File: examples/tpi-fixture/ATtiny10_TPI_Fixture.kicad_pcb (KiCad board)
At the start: 2 copper layers, 76.2 x 63.5 mm, 25 parts, among them J1 USBasp ISP (2x5 box header), J2 CNV-SOT23-6L-DIP carrier, SW1A 4PDT on-on (pole A), SW1B 4PDT on-on (pole B), SW1C 4PDT on-on (pole C), SW1D 4PDT on-on (pole D), SW2 MODE NORMAL/HV, SW3 HV POWER, SW4 HV ENABLE (guarded)

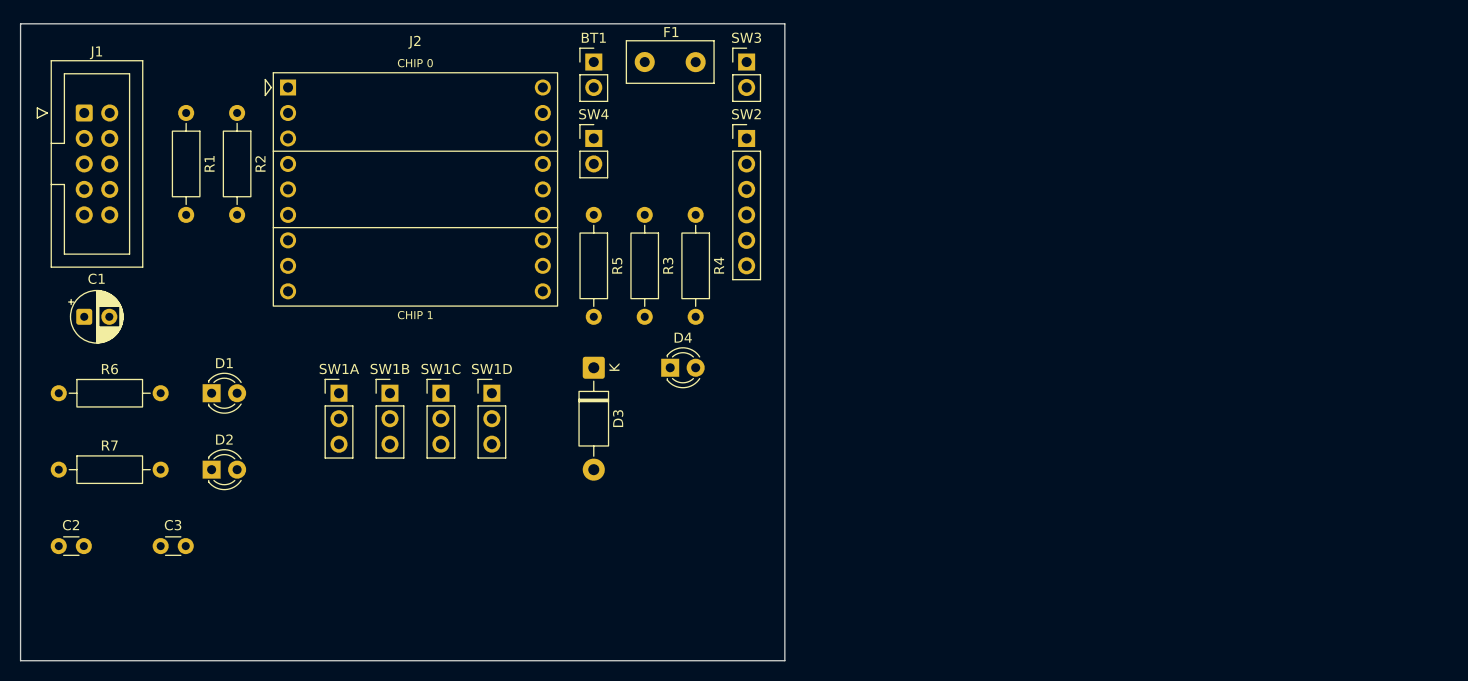
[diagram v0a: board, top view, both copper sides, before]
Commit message: Make examples/tpi-fixture the real-parts board (fixture by Mildrew) and test it
The board and netlist are Mildrew's real-parts version (22 footprints, 86 pads, 41 nets), copied
byte-exactly. New tests: all 22 parts snap with examples/x56.toml, BT1 passes as slotted (and is
rejected without it), 0 conflicts, the netlist matches, and the X56 grid-width warning is present
(the outline is still 30 holes wide).
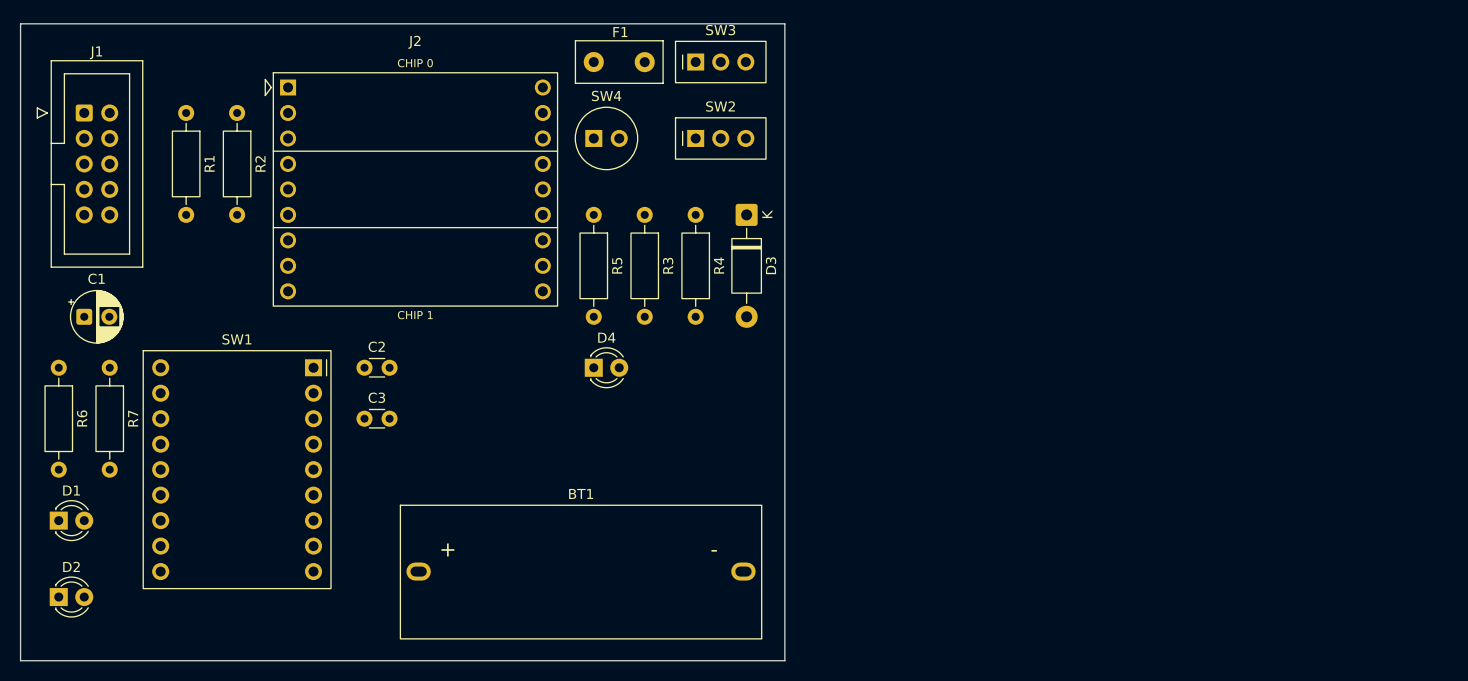
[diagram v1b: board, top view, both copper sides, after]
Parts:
- removed SW1A: 4PDT on-on (pole A), Connector_PinHeader_2.54mm:PinHeader_1x03_P2.54mm_Vertical
- removed SW1B: 4PDT on-on (pole B), Connector_PinHeader_2.54mm:PinHeader_1x03_P2.54mm_Vertical
- removed SW1C: 4PDT on-on (pole C), Connector_PinHeader_2.54mm:PinHeader_1x03_P2.54mm_Vertical
- removed SW1D: 4PDT on-on (pole D), Connector_PinHeader_2.54mm:PinHeader_1x03_P2.54mm_Vertical
- added SW1: CHIP SEL 6PDT (MSS6200 on adapter), ATtiny10_TPI_Fixture:MSS6200_Adapter_2x09_P2.54mm, F.Cu at (79.2, 84.3)
- BT1: value 12V (23A or 8xAA pack) -> 12V 23A cell (MPD BH23APC); footprint Connector_PinHeader_2.54mm:PinHeader_1x02_P2.54mm_Vertical -> ATtiny10_TPI_Fixture:BatteryHolder_MPD_BH23APC_1x23A_Stripboard_H0-H13
- SW2: footprint Connector_PinHeader_2.54mm:PinHeader_1x06_P2.54mm_Vertical -> ATtiny10_TPI_Fixture:SW_Slide_SPDT_SS12D00G_P2.50mm_Vertical
- SW3: footprint Connector_PinHeader_2.54mm:PinHeader_1x02_P2.54mm_Vertical -> ATtiny10_TPI_Fixture:SW_Slide_SPDT_SS12D00G_P2.50mm_Vertical
- SW4: footprint Connector_PinHeader_2.54mm:PinHeader_1x02_P2.54mm_Vertical -> ATtiny10_TPI_Fixture:SW_Push_Round_D6mm_1x02_P2.54mm_PROVISIONAL
- moved BT1 53.8 mm to (89.4, 104.6)
- moved C2 35.3 mm to (84.3, 84.3)
- moved C3 24.0 mm to (84.3, 89.4)
- moved D3 21.6 mm to (122.4, 69.0)
- moved D1 19.8 mm to (53.8, 99.5)
- moved D2 19.8 mm to (53.8, 107.2)
- moved R7 11.4 mm to (58.9, 84.3), turned to -90 degrees
- moved D4 7.62 mm to (107.2, 84.3)
- moved F1 5.08 mm to (107.2, 53.8)
- moved SW2 5.08 mm to (117.3, 61.4)
- moved SW3 5.08 mm to (117.3, 53.8)
- moved R6 2.54 mm to (53.8, 84.3), turned to -90 degrees
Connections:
- F1 pad 2: Net-(SW3-A) -> Net-(SW3-B)
- R3 pad 1: /SCHEMATIC DIAGRAM/HV_ARMED -> /SCHEMATIC DIAGRAM/HV_SW
- SW4 pad 1: Net-(SW3-B) -> Net-(SW3-A)

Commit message: Update the real-parts fixture: X56 outline, BT1 up one strip (fixture by Mildrew)
Mildrew widened the Edge.Cuts outline to Kevin's X56 board (56 x 24 holes, A1-X56) and moved BT1
up one strip (slot jobs now on strip U). The X56 grid-width warning is gone; build writes the
full 56-hole strips (1226 tracks). Tests and the fixture README updated.
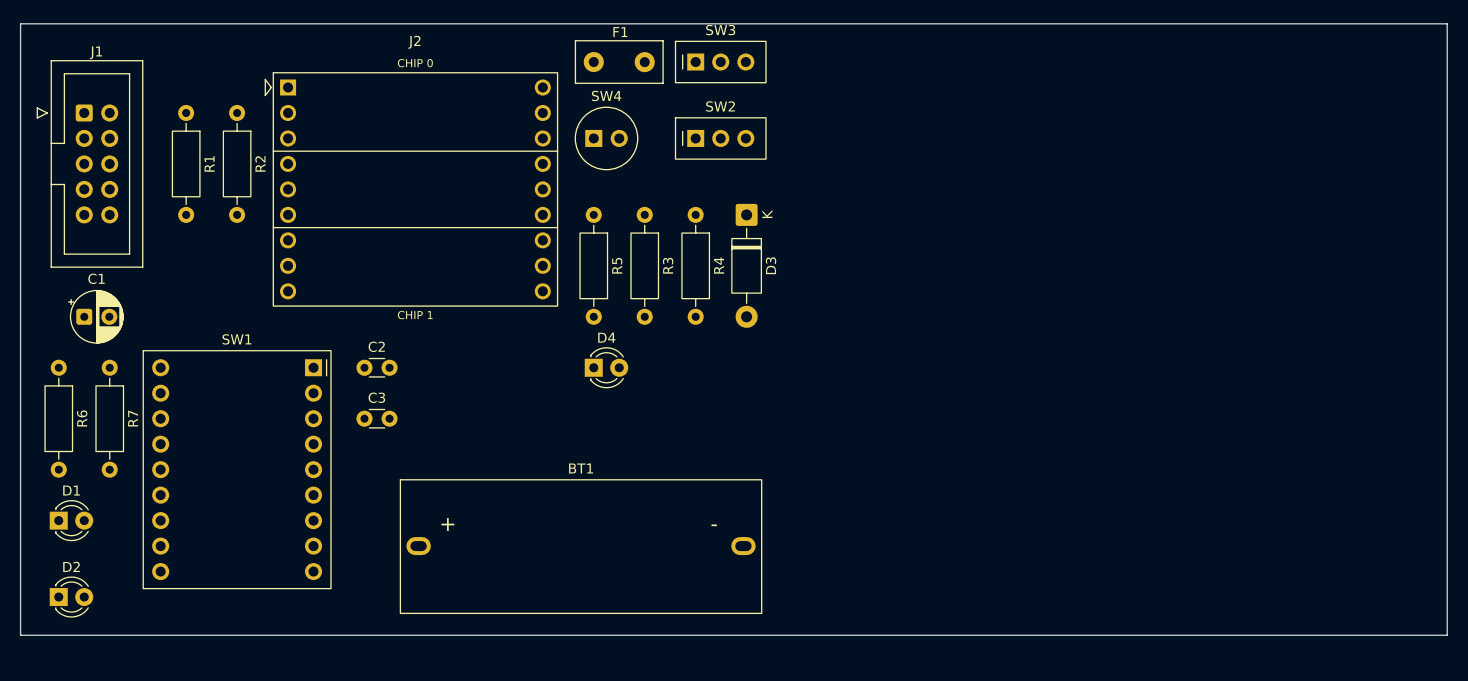
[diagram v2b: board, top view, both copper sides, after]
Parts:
- moved BT1 2.54 mm to (89.4, 102.1)
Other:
- board size 76.2 x 63.5 mm -> 142.2 x 61 mm
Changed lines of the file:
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@@
 	(footprint "ATtiny10_TPI_Fixture:BatteryHolder_MPD_BH23APC_1x23A_Stripboard_H0-H13"
 		(layer "F.Cu")
-		(at 89.37 104.61)
+		(at 89.37 102.07)
 		(descr "MPD BH23APC 23A battery holder with PC pins (flat tabs 0.50x1.00 mm, true spacing 31.70 mm), stripboard build: pins on ONE strip at grid holes 0 and 13 (33.02 mm), each end hole filed 0.635 mm (0.025in) inward -> pin centres 31.75 mm. Oval slots start at the grid hole and extend 0.635 mm inboard. CUT THE STRIP BETWEEN THE PINS. Pad 1 = + (end away from the spring). Centre mounting hole omitted. Source: MPD drawing BH23APC rev F 2/09/18.")
 		(tags "battery holder 23A A23 MPD BH23APC stripboard")
@@
 	(gr_rect
 		(start 50 50)
-		(end 126.2 113.5)
+		(end 192.24 110.96)
 		(stroke
 			(width 0.1)
